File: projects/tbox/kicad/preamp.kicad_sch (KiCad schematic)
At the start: 26 parts, among them J1101 MIC 3.5, J1102 MIC 1/4, J1103 HEADSET, J1104 SPARE, U1101 OPA1678, U1102 TS12A12511

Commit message: Headset TRRS jacks: Same Sky/CUI SJ-43514 with a project footprint
The SJ1-3535NG assigned in the footprint pass is a 3-conductor jack with
switches; the headset symbol (AudioJack4: T/R1/R2/S, CTIA, mic on the
sleeve) needs an isolated 4-conductor part. SJ-43514: plastic bushing,
4 conductors, no switch. Footprint from the SJ-4351X drawing; pins 3/5
depth scaled (undimensioned) - on the verify-before-order list.
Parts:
- J1103: footprint Connector_Audio:Jack_3.5mm_CUI_SJ1-3535NG_Horizontal -> tbox:Jack_3.5mm_CUI_SJ-43514_Horizontal; MPN SJ1-3535NG -> SJ-43514
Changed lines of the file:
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@@
 			)
 		)
-		(property "Footprint" "Connector_Audio:Jack_3.5mm_CUI_SJ1-3535NG_Horizontal"
+		(property "Footprint" "tbox:Jack_3.5mm_CUI_SJ-43514_Horizontal"
 			(at 27.94 68.58 0)
 			(hide yes)
@@
 			)
 		)
-		(property "MPN" "SJ1-3535NG"
+		(property "MPN" "SJ-43514"
 			(at 27.94 68.58 0)
 			(hide yes)

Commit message: Review fixes, tooling: parts stay on their board, panel datums, V-cut keepouts, regulator caps, stricter checkers
- place_panel: rear board is 180..270 (was 250); cluster and refinement
  placement can no longer cross a V-score; top-panel parts are placed by
  their shaft/plunger datum (DATUM table), not the footprint origin.
- New tools/check_placement.py: every footprint inside its board's band
  (jack noses may overhang the outer edges) and no non-power net spans
  boards without a ribbon connector. Board re-placed: 0 problems, no
  courtyard overlaps.
- setup_pcb: copper keepout rule areas +-1 mm about each V-score on all
  four copper layers (tracks, vias, pads, fills).
- place_decoupling: band by the cap's own board; targets are power pins
  only (SENSE/EN excluded, from the netlist); converters get the bulk caps
  on their rails first -- C2513 is now at the TPS7A4701 OUT pin.
- power_model/check_power: Load_mA must parse as finite, non-negative,
  typ<=max; any part with a power_in pin on a rail must carry one; an
  empty netlist or any model warning fails the check. The five
  TS12A12511s get Load_mA 0/0.01.
- gen_power_tree: strip_managed walks parens string-aware.
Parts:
- U1102: Load_mA (none) -> 0/0.01
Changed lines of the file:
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@@
+			)
+		)
+		(property "Load_mA" "0/0.01"
+			(at 246.38 114.3 0)
+			(show_name no)
+			(do_not_autoplace no)
+			(hide yes)
+			(effects
+				(font
+					(size 1.27 1.27)
+				)
 			)
 		)
@@
 			(effects
 				(font
+					(size 1.27 1.27)
+				)
+			)
+		)
+		(property "Load_mA" "0/0.01"
+			(at 156.21 55.88 0)
+			(show_name no)
+			(do_not_autoplace no)
+			(hide yes)
+			(effects
+				(font

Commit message: Preamp: LO +28 / HI +40 dB, mic on tip with bias on tip and ring, TRRS return to chassis, ESD arrays at the jacks
Review Q6/Q9/Q1/Q8: R1104 1k1->430R (stage 1 +27.7 dB), R1106 1k1->3k3
(stage 2 +12 dB); the tip-ring strap on the 3.5 mm mic jack is gone --
mic on the tip, the ring gets its own 2k2 bias feed (R1109) with an RF
shunt (C1109), so TS plugs no longer ground the mic and PC headsets that
expect ring bias work; the TRRS ring 2 (headset return) lands on CHASSIS;
two SP724 clamp arrays (new tbox:SP724 symbol) sit on the six jack
contacts.
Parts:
- added C1109: 1n, Capacitor_SMD:C_0603_1608Metric, symbol Device:C
- added R1109: 2k2, Resistor_SMD:R_0603_1608Metric, symbol Device:R
- added U1103, U1104: SP724, Package_TO_SOT_SMD:SOT-23-6, symbol tbox:SP724
- R1104: value 1k1 -> 430R
- R1106: value 1k1 -> 3k3
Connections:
- net +9V: now also U1103.5 (V+), U1104.5 (V+)
- net BIAS_IN: now also R1109.1
- net CHASSIS: now also J1103.R2
- net GND: now also C1109.2, U1103.2 (V-), U1104.2 (V-); no longer J1103.R2
- net PH_L: now also U1104.1 (IN1)
- net PH_R: now also U1104.3 (IN2)
- net MIC14T: now reaches FB1102.1, J1102.T
- net MIC14T: now also U1103.4 (IN3)
- net MIC35T: now reaches FB1101.1, J1101.T
- net MIC35T: now also U1103.1 (IN1); no longer J1101.R
- net HS_MIC: now reaches FB1103.1, J1103.S
- net HS_MIC: now also U1103.6 (IN4)
- new net MIC_R: C1109.1, J1101.R, R1109.2, U1103.3 (IN2)
- no-connect marks 0 -> 2

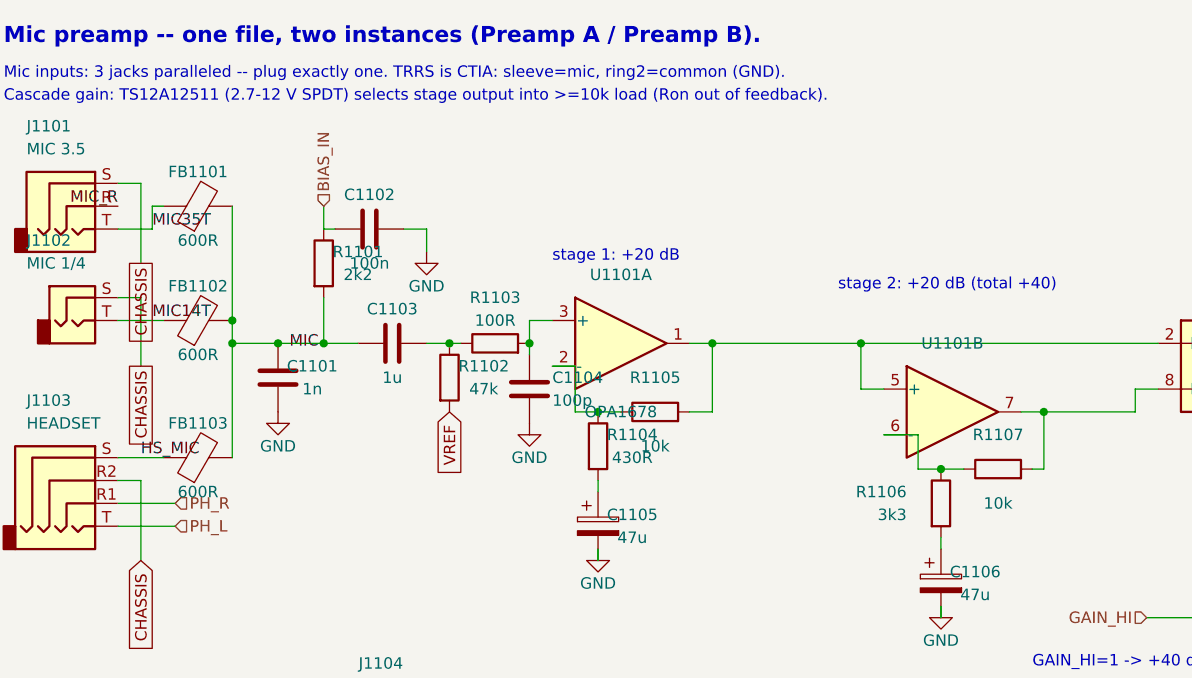
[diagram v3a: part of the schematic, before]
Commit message: Review design changes: chassis returns, OPA1622 phones amps, RX-in protection, supervisor, mute fade, gains, BLEND buffer, jack-side protection, mic-jack bias
Decisions Q1-Q9 from the 2026-09-08 adversarial review:
- Q1 (D): phones jack sleeves and TRRS ring 2 on CHASSIS; GND-CHASSIS
  ties per board (NT1001 front at the headset jacks, NT2401 control at
  the phones amps, NT3201 rear) with chassis studs H1001/H2401; phones
  return rides the chassis, never the ribbon ground.
- Q2 (B'): U2401/U2403 NJM4556A -> OPA1622 (new tbox symbol, VSON-10),
  build-out 10R -> 3R3, EN from PWR_OK.
- Q3 (A+C): RX-in coupling caps non-polar 10u, 2k2 series, 1N4148W
  clamps to the rails at the op-amp inputs (SMAJ15CA stays at the jack).
- Q4 (B): TPS3808G01 supervisor on +9 V (7.5 V, ~1.2 s) -> PWR_OK;
  MUTE_HOLD inverter replaces the RC hold, shunts PTT_ACTIVE; Q3201 gets
  a 100k gate pull-down.
- Q5 (A): mute fades (2k2 + back-to-back 2N7002 shunt to Vref, ~5 ms)
  before the TS12A12511 switches (~30 ms, immediate release).
- Q6 (A): preamp LO +28 / HI +40 dB (R1104 430R, R1106 3k3).
- Q7 (A): BLEND is an inverting summer on U3301B (R3318 22k, C3317).
- Q8 (C): phones RF filters move to the front board at the jacks; SP724
  arrays on every front jack contact and the rear PTT inputs; SMAJ15CA
  across each isolated line-out secondary.
- Q9 (B'): 3.5 mm mic jack tip carries the mic, tip and ring both get
  2k2 bias (R1109/C1109).
DESIGN.md, LEVELS.md and TODO.md updated; ERC 0, check_sch/boards/
footprints/power clean; power tree regenerated.
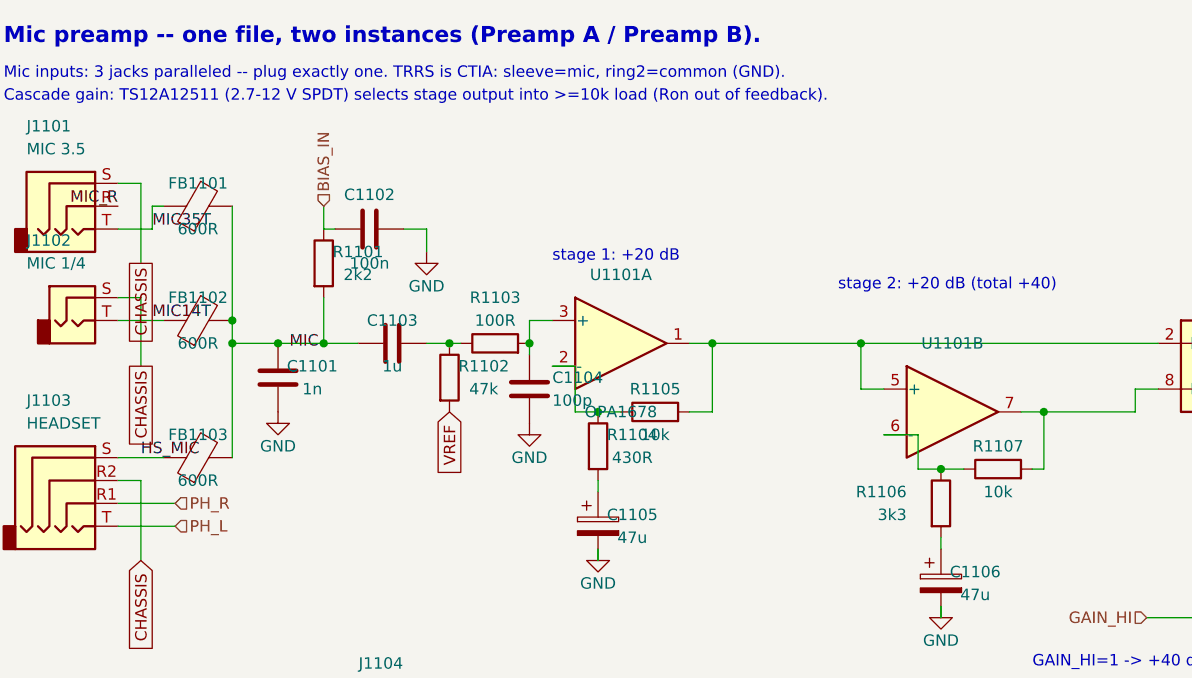
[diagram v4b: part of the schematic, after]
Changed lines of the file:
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@@
 		(dnp no)
 		(property "Reference" "R1105"
-			(at 92.71 57.15 90)
+			(at 92.71 58.42 90)
 			(show_name no)
 			(do_not_autoplace no)
@@
 		)
 		(property "Value" "10k"
-			(at 92.71 64.77 90)
+			(at 92.71 63.5 90)
 			(show_name no)
 			(do_not_autoplace no)
@@
 		(dnp no)
 		(property "Reference" "C1103"
-			(at 63.5 49.53 90)
+			(at 63.5 50.8 90)
 			(show_name no)
 			(do_not_autoplace no)
@@
 		)
 		(property "Value" "1u"
-			(at 63.5 57.15 90)
+			(at 63.5 55.88 90)
 			(show_name no)
 			(do_not_autoplace no)
@@
 		(dnp no)
 		(property "Reference" "FB1103"
-			(at 41.91 62.23 90)
+			(at 41.91 63.5 90)
 			(show_name no)
 			(do_not_autoplace no)
@@
 		)
 		(property "Value" "600R"
-			(at 41.91 69.85 90)
+			(at 41.91 68.58 90)
 			(show_name no)
 			(do_not_autoplace no)
@@
 		(dnp no)
 		(property "Reference" "FB1101"
-			(at 41.91 34.29 90)
+			(at 41.91 35.56 90)
 			(show_name no)
 			(do_not_autoplace no)
@@
 		)
 		(property "Value" "600R"
-			(at 41.91 41.91 90)
+			(at 41.91 40.64 90)
 			(show_name no)
 			(do_not_autoplace no)
@@
 		(dnp no)
 		(property "Reference" "R1107"
-			(at 130.81 63.5 90)
+			(at 130.81 64.77 90)
 			(show_name no)
 			(do_not_autoplace no)
@@
 		)
 		(property "Value" "10k"
-			(at 130.81 71.12 90)
+			(at 130.81 69.85 90)
 			(show_name no)
 			(do_not_autoplace no)
@@
 		(dnp no)
 		(property "Reference" "FB1102"
-			(at 41.91 46.99 90)
+			(at 41.91 48.26 90)
 			(show_name no)
 			(do_not_autoplace no)
@@
 		)
 		(property "Value" "600R"
-			(at 41.91 54.61 90)
-			(show_name no)
-			(do_not_autoplace no)
+			(at 41.91 53.34 90)
+			(show_name no)
+			(do_not_autoplace no)

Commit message: Review 2 fixes: PWR_OK pull-up and supervisor bypass on the 5 V rail, CT 220n, ring-bias load, ribbon reach check, doc contradictions
- TPS3808 RESET is rated 6.5 V (7 V abs max): R2507 now pulls PWR_OK up to
  BIAS_5V, which is also VDD; C2517 100n bypasses VDD at the part.
- C2516 220n: tD = CT(nF)/175 + 0.5 ms, so 1u was 5.7 s, not 1.2 s.
- R1109/R1309 ring-bias resistors carry Load_mA 0/1 on BIAS_5V.
- C2513 47u X7R 25V, MPN GRM32ER71E476KE15L.
- check_placement: a net that spans boards must reach every one of them
  through a cable present at both ends, not just touch any ribbon.
- DESIGN.md: Vref is the mute/summing reference, not DC bias only; three
  chassis ties, not NT3201 alone; supervisor text matches the schematic.
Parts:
- R1109: Load_mA (none) -> 0/1; Load_rail (none) -> BIAS_5V
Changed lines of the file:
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@@
+			)
+		)
+		(property "Load_mA" "0/1"
+			(at 38.1 152.4 0)
+			(show_name no)
+			(do_not_autoplace no)
+			(hide yes)
+			(effects
+				(font
+					(size 1.27 1.27)
+				)
+			)
+		)
+		(property "Load_rail" "BIAS_5V"
+			(at 38.1 152.4 0)
+			(show_name no)
+			(do_not_autoplace no)
+			(hide yes)
+			(effects
+				(font
+					(size 1.27 1.27)
+				)
 			)
 		)

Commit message: Review 2: load maxima and the resistor rule
- Op-amp maxima from the datasheets: OPA1678 duals 4/6 (5.6 mA IQ over
  temperature), line drivers 4/10, OPA1622 6/101 (8.4 mA IQ + two
  145 mA-peak class-B channels).
- Every resistor with an end on a rail now needs Load_mA (Vref returns
  and the ADP7142 output RC exempt): R2122, R2501, R2505, R2507,
  R3209/R3210 (1k gain-select pull-ups, 9 mA each when closed),
  R3201/R3202 PTT pull-ups annotated.
- Load_mA syntax is strict (n or n/m).
- RAW_13V8 capability 400 mA (1812L050 hold at 50 C), not 500.
- C3401/C3402 10u X7R 25V, GRM31CR71E106KA12L.
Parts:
- U1101: Load_mA (none) -> 4/6
- U1101: Load_mA 4/5 -> 4/6
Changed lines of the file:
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@@
+			)
+		)
+		(property "Load_mA" "4/6"
+			(at 231.14 111.76 0)
+			(show_name no)
+			(do_not_autoplace no)
+			(hide yes)
+			(effects
+				(font
+					(size 1.27 1.27)
+				)
 			)
 		)
@@
 			)
 		)
-		(property "Load_mA" "4/5"
+		(property "Load_mA" "4/6"
 			(at 88.9 45.72 0)
 			(hide yes)

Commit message: Review 2 design decisions: mute cell sequencing, phones precharge, non-inverting BLEND, chassis RF returns, SP724 bypass and placement, TVS ahead of the bead, load and level updates
Q1  Mute cell: MUTE is a source-only OR with a 100k pull-down; a 2N7002
    inverter (Q1203) and sink (Q1204) pull SW_CTL hard low on release so
    the SPDT reconnects under the shunt, the fade gate charges through
    D1201/47k and bleeds through 470k (~50 ms); nothing discharges
    through MUTE any more.
Q2  1k from Vref on each OPA1622 output node (R2425-R2428) precharges
    the 470u phones caps during the hold.
Q3  Fade resistor 220R (all three instances): 0.2 dB insertion, TX_MIX
    level within 0.3 dB of the line-out jumpering.
Q4  LO stays +28 dB; -28 dBV desk mics declared out of scope in LEVELS.
Q5  SP724s stay on the rails, each with its own 100n (C1110/C1111/C1007/
    C3208 + B copies), placed behind their jack (place_panel ATTACH,
    check_placement 20 mm rule); mic RF caps C1101/C1109 return to
    CHASSIS.
Q6  Supply source envelope documented (bench/rig PSU, fused at source);
    SMBJ18A moved to the post-Schottky node ahead of FB2501; TODO for
    mobile use.
Q7  BLEND is a non-inverting summer (22k/22k into +IN, R3319 22k to Vref
    for a gain of 2), in phase with the RX selections.
Q8  Key-inhibit delay through MUTE_HOLD accepted and documented.
Q9  Beads are Murata BLM21PG601SN1D (600 R, 1.4 A, 0.14 R; datasheet
    added); PVA ordering code TODO names the panel gap that sets it.
Also: setup_pcb cuts the SJ-43514 4.5 x 1.3 mm edge notches at the jacks
on the board; supervisor hold text 1.3 s.
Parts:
- added C1110, C1111: 100n, Capacitor_SMD:C_0603_1608Metric, symbol Device:C
- FB1101, FB1102, FB1103: MPN (none) -> BLM21PG601SN1D
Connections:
- net +9V: now also C1110.1, C1111.1
- net CHASSIS: now also C1101.2, C1109.2
- net GND: now also C1110.2, C1111.2; no longer C1101.2, C1109.2
